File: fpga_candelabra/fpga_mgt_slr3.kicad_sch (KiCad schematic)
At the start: 1 part, among them U1 XCVU13P-B2104

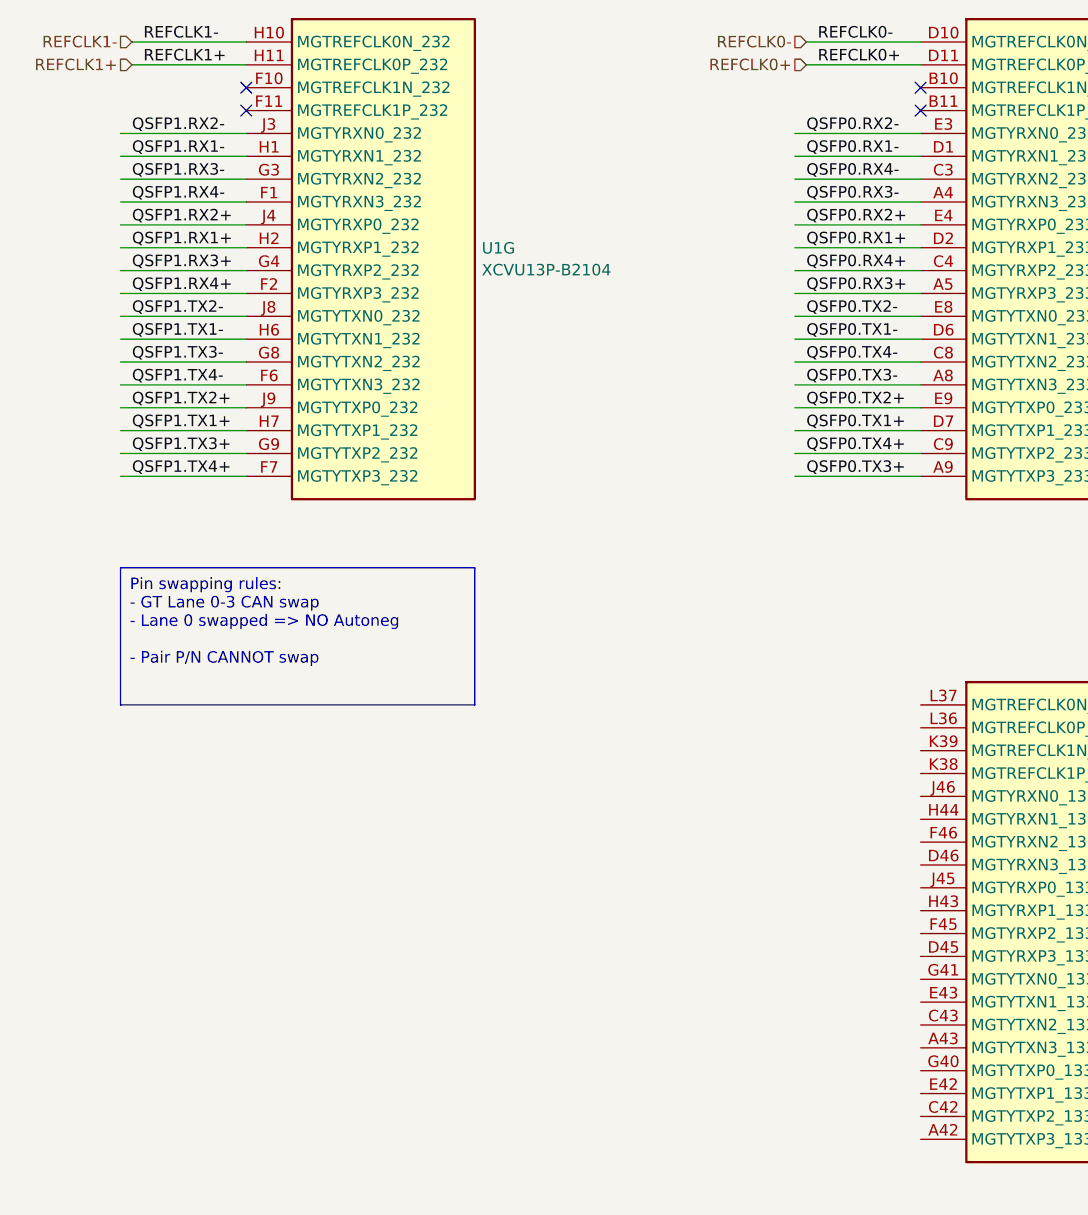
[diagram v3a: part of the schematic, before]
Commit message: fpga_candelabra: sch & layout v0.5, pass basic ERC & DRC
Signed-off-by: Yichuan Gao <gaoyichuan000@gmail.com>
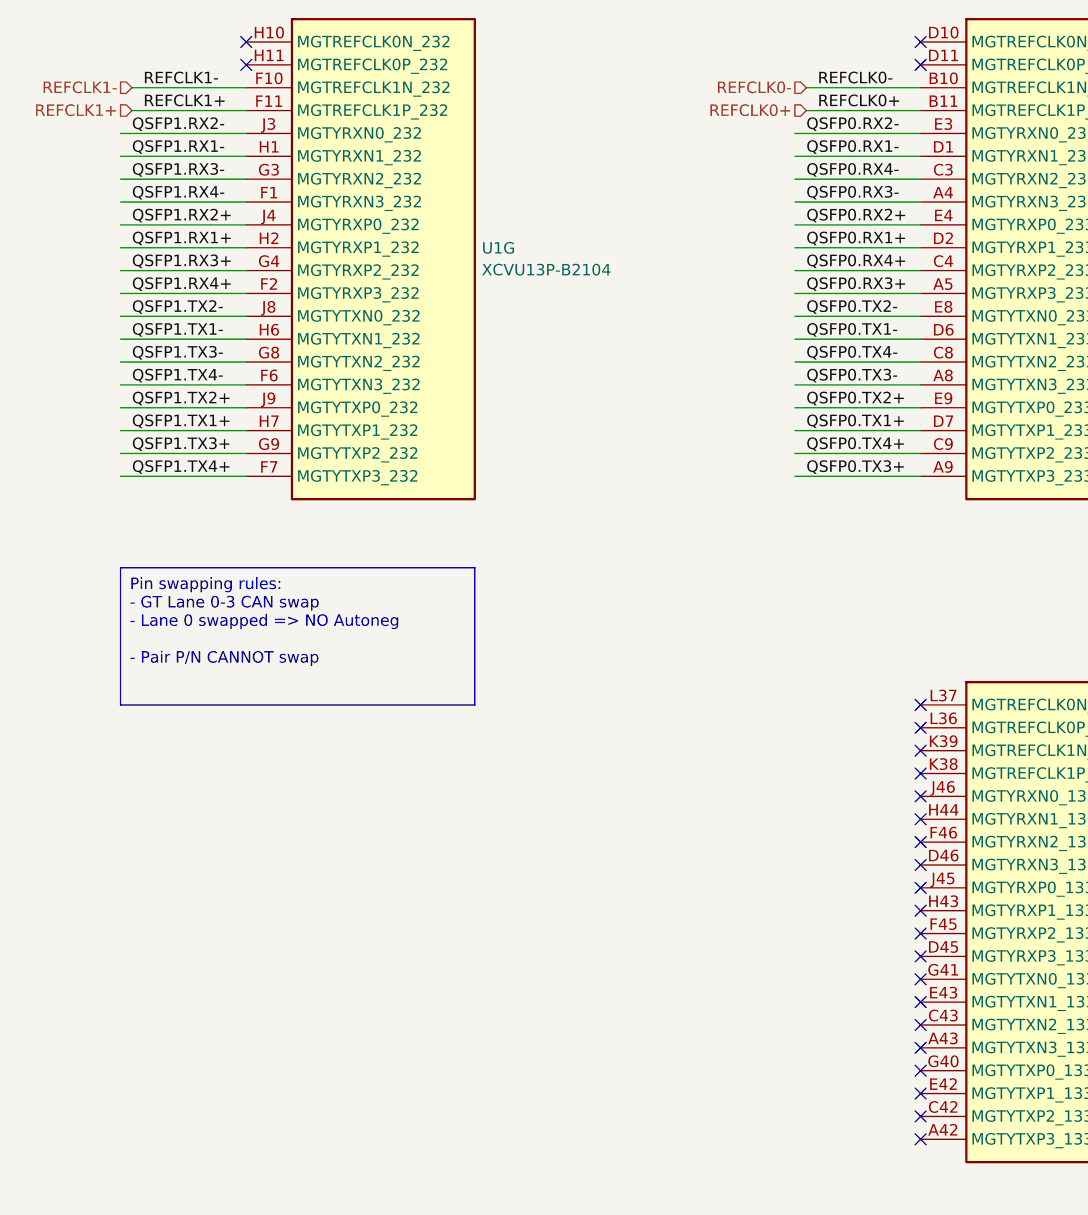
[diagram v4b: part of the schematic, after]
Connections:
- net REFCLK0+: now also U1.B11 (MGTREFCLK1P_233); no longer U1.D11 (MGTREFCLK0P_233)
- net REFCLK0-: now also U1.B10 (MGTREFCLK1N_233); no longer U1.D10 (MGTREFCLK0N_233)
- net REFCLK1+: now also U1.F11 (MGTREFCLK1P_232); no longer U1.H11 (MGTREFCLK0P_232)
- net REFCLK1-: now also U1.F10 (MGTREFCLK1N_232); no longer U1.H10 (MGTREFCLK0N_232)
- no-connect marks 4 -> 24
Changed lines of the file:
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@@
 	(paper "A4")
 	(no_connect
-		(at 45.72 41.91)
-	)
-	(no_connect
-		(at 120.65 39.37)
-	)
-	(no_connect
-		(at 45.72 39.37)
-	)
-	(no_connect
-		(at 120.65 41.91)
+		(at 120.65 115.57)
+	)
+	(no_connect
+		(at 120.65 125.73)
+	)
+	(no_connect
+		(at 120.65 118.11)
+	)
+	(no_connect
+		(at 45.72 36.83)
+	)
+	(no_connect
+		(at 120.65 140.97)
+	)
+	(no_connect
+		(at 120.65 107.95)
+	)
+	(no_connect
+		(at 120.65 146.05)
+	)
+	(no_connect
+		(at 120.65 148.59)
+	)
+	(no_connect
+		(at 120.65 128.27)
+	)
+	(no_connect
+		(at 120.65 110.49)
+	)
+	(no_connect
+		(at 120.65 156.21)
+	)
+	(no_connect
+		(at 120.65 138.43)
+	)
+	(no_connect
+		(at 120.65 123.19)
+	)
+	(no_connect
+		(at 120.65 143.51)
+	)
+	(no_connect
+		(at 120.65 34.29)
+	)
+	(no_connect
+		(at 120.65 113.03)
+	)
+	(no_connect
+		(at 120.65 120.65)
+	)
+	(no_connect
+		(at 120.65 130.81)
+	)
+	(no_connect
+		(at 45.72 34.29)
+	)
+	(no_connect
+		(at 120.65 151.13)
+	)
+	(no_connect
+		(at 120.65 133.35)
+	)
+	(no_connect
+		(at 120.65 36.83)
+	)
+	(no_connect
+		(at 120.65 153.67)
+	)
+	(no_connect
+		(at 120.65 135.89)
 	)
 	(wire
@@
 	(wire
 		(pts
-			(xy 33.02 36.83) (xy 45.72 36.83)
+			(xy 33.02 41.91) (xy 45.72 41.91)
 		)
 		(stroke
@@
 	(wire
 		(pts
-			(xy 107.95 34.29) (xy 120.65 34.29)
+			(xy 107.95 39.37) (xy 120.65 39.37)
 		)
 		(stroke
@@
 	(wire
 		(pts
-			(xy 33.02 34.29) (xy 45.72 34.29)
+			(xy 33.02 39.37) (xy 45.72 39.37)
 		)
 		(stroke
@@
 	(wire
 		(pts
-			(xy 107.95 36.83) (xy 120.65 36.83)
+			(xy 107.95 41.91) (xy 120.65 41.91)
 		)
 		(stroke
@@
 	)
 	(label "REFCLK0-"
-		(at 109.22 34.29 0)
+		(at 109.22 39.37 0)
 		(fields_autoplaced yes)
 		(effects
@@
 	)
 	(label "REFCLK1+"
-		(at 34.29 36.83 0)
+		(at 34.29 41.91 0)
 		(fields_autoplaced yes)
 		(effects
@@
 	)
 	(label "REFCLK1-"
-		(at 34.29 34.29 0)
+		(at 34.29 39.37 0)
 		(fields_autoplaced yes)
 		(effects
@@
 	)
 	(label "REFCLK0+"
-		(at 109.22 36.83 0)
+		(at 109.22 41.91 0)
 		(fields_autoplaced yes)
 		(effects
@@
 	(hierarchical_label "REFCLK0+"
 		(shape input)
-		(at 107.95 36.83 180)
+		(at 107.95 41.91 180)
 		(fields_autoplaced yes)
 		(effects
@@
 	(hierarchical_label "REFCLK1-"
 		(shape input)
-		(at 33.02 34.29 180)
+		(at 33.02 39.37 180)
 		(fields_autoplaced yes)
 		(effects
@@
 	(hierarchical_label "REFCLK1+"
 		(shape input)
-		(at 33.02 36.83 180)
+		(at 33.02 41.91 180)
 		(fields_autoplaced yes)
 		(effects
@@
 	(hierarchical_label "REFCLK0-"
 		(shape input)
-		(at 107.95 34.29 180)
-		(fields_autoplaced yes)
-		(effects
+		(at 107.95 39.37 180)
+		(fields_autoplaced yes)
+		(effects

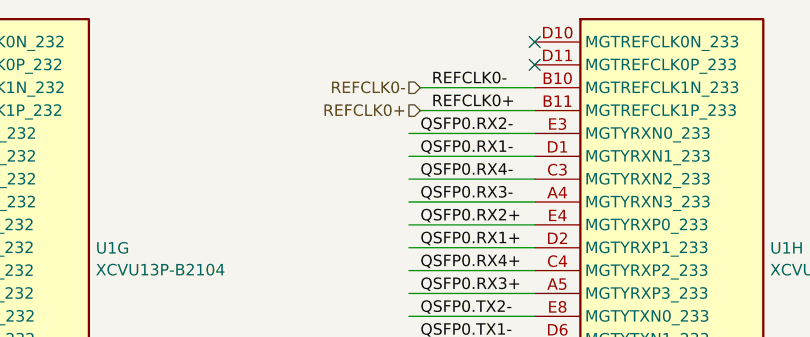
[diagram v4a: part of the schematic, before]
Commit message: fpga_candelabra: more bugfixes & improvements for rev 0.2.0
- Add Digilent JTAG-SMT2-NC onboard
- Add fan controller & 4pin fan header
- Use 9pin header for USB2.0
- Misc fixes for structure

Signed-off-by: Yichuan Gao <gaoyichuan000@gmail.com>
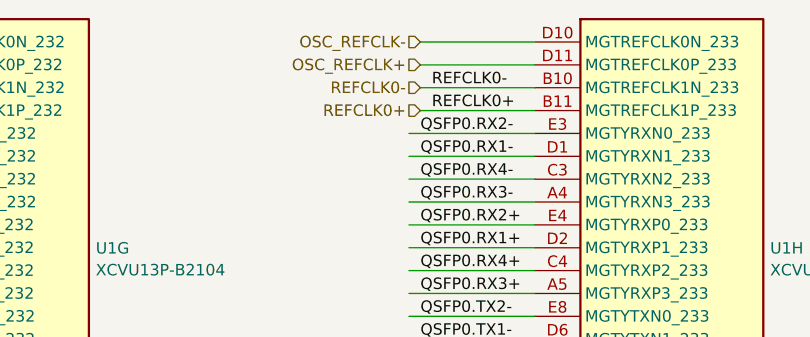
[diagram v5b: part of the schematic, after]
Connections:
- net OSC_REFCLK-: now reaches U1.D10 (MGTREFCLK0N_233)
- net OSC_REFCLK+: now reaches U1.D11 (MGTREFCLK0P_233)
- no-connect marks 24 -> 22
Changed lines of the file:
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@@
-	)
-	(no_connect
-		(at 120.65 34.29)
 	)
 	(no_connect
@@
 	)
 	(no_connect
-		(at 120.65 36.83)
-	)
-	(no_connect
 		(at 120.65 153.67)
 	)
@@
 	(wire
 		(pts
+			(xy 107.95 36.83) (xy 120.65 36.83)
+		)
+		(stroke
+			(width 0)
+			(type default)
+		)
+	)
+	(wire
+		(pts
 			(xy 106.68 82.55) (xy 120.65 82.55)
 		)
@@
 		(pts
 			(xy 31.75 57.15) (xy 45.72 57.15)
+		)
+		(stroke
+			(width 0)
+			(type default)
+		)
+	)
+	(wire
+		(pts
+			(xy 107.95 34.29) (xy 120.65 34.29)
 		)
 		(stroke
@@
 	(label "QSFP1.RX2+"
 		(at 33.02 54.61 0)
-		(fields_autoplaced yes)
 		(effects
 			(font
@@
 	(label "QSFP0.RX2+"
 		(at 107.95 54.61 0)
-		(fields_autoplaced yes)
 		(effects
 			(font
@@
 	(label "QSFP0.TX1-"
 		(at 107.95 67.31 0)
-		(fields_autoplaced yes)
 		(effects
 			(font
@@
 	(label "QSFP0.TX2+"
 		(at 107.95 74.93 0)
-		(fields_autoplaced yes)
 		(effects
 			(font
@@
 	(label "QSFP0.RX4-"
 		(at 107.95 49.53 0)
-		(fields_autoplaced yes)
 		(effects
 			(font
@@
 	(label "QSFP1.RX3+"
 		(at 33.02 59.69 0)
-		(fields_autoplaced yes)
 		(effects
 			(font
@@
 	(label "QSFP0.TX2-"
 		(at 107.95 64.77 0)
-		(fields_autoplaced yes)
 		(effects
 			(font
@@
 	(label "QSFP1.RX1+"
 		(at 33.02 57.15 0)
-		(fields_autoplaced yes)
 		(effects
 			(font
@@
 	(label "QSFP0.TX4+"
 		(at 107.95 80.01 0)
-		(fields_autoplaced yes)
 		(effects
 			(font
@@
 	(label "QSFP1.TX3-"
 		(at 33.02 69.85 0)
-		(fields_autoplaced yes)
 		(effects
 			(font
@@
 	(label "QSFP1.RX2-"
 		(at 33.02 44.45 0)
-		(fields_autoplaced yes)
 		(effects
 			(font
@@
 	(label "QSFP0.RX1+"
 		(at 107.95 57.15 0)
-		(fields_autoplaced yes)
 		(effects
 			(font
@@
 	(label "QSFP0.TX4-"
 		(at 107.95 69.85 0)
-		(fields_autoplaced yes)
 		(effects
 			(font
@@
 	(label "QSFP1.TX1+"
 		(at 33.02 77.47 0)
-		(fields_autoplaced yes)
 		(effects
 			(font
@@
 	(label "QSFP0.TX1+"
 		(at 107.95 77.47 0)
-		(fields_autoplaced yes)
 		(effects
 			(font
@@
 	(label "QSFP0.TX3+"
 		(at 107.95 82.55 0)
-		(fields_autoplaced yes)
 		(effects
 			(font
@@
 	(label "QSFP0.RX3+"
 		(at 107.95 62.23 0)
-		(fields_autoplaced yes)
 		(effects
 			(font
@@
 	(label "REFCLK0-"
 		(at 109.22 39.37 0)
-		(fields_autoplaced yes)
 		(effects
 			(font
@@
 	(label "QSFP1.TX1-"
 		(at 33.02 67.31 0)
-		(fields_autoplaced yes)
 		(effects
 			(font
@@
 	(label "REFCLK1+"
 		(at 34.29 41.91 0)
-		(fields_autoplaced yes)
 		(effects
 			(font
@@
 	(label "QSFP1.RX4+"
 		(at 33.02 62.23 0)
-		(fields_autoplaced yes)
 		(effects
 			(font
@@
 	(label "QSFP1.TX2+"
 		(at 33.02 74.93 0)
-		(fields_autoplaced yes)
 		(effects
 			(font
@@
 	(label "QSFP1.TX4+"
 		(at 33.02 82.55 0)
-		(fields_autoplaced yes)
 		(effects
 			(font
@@
 	(label "QSFP0.TX3-"
 		(at 107.95 72.39 0)
-		(fields_autoplaced yes)
 		(effects
 			(font
@@
 	(label "REFCLK1-"
 		(at 34.29 39.37 0)
-		(fields_autoplaced yes)
 		(effects
 			(font
@@
 	(label "QSFP1.RX1-"
 		(at 33.02 46.99 0)
-		(fields_autoplaced yes)
 		(effects
 			(font
@@
 	(label "QSFP0{QSFP}"
 		(at 265.43 157.48 0)
-		(fields_autoplaced yes)
 		(effects
 			(font
@@
 	(label "QSFP0.RX4+"
 		(at 107.95 59.69 0)
-		(fields_autoplaced yes)
 		(effects
 			(font
@@
 	(label "QSFP1.TX2-"
 		(at 33.02 64.77 0)
-		(fields_autoplaced yes)
 		(effects
 			(font
@@
 	(label "REFCLK0+"
 		(at 109.22 41.91 0)
-		(fields_autoplaced yes)
 		(effects
 			(font
@@
 	(label "QSFP1.TX4-"
 		(at 33.02 72.39 0)
-		(fields_autoplaced yes)
 		(effects
 			(font
@@
 	(label "QSFP0.RX2-"
 		(at 107.95 44.45 0)
-		(fields_autoplaced yes)
 		(effects
 			(font
@@
 	(label "QSFP0.RX3-"
 		(at 107.95 52.07 0)
-		(fields_autoplaced yes)
 		(effects
 			(font
@@
 	(label "QSFP1{QSFP}"
 		(at 265.43 161.29 0)
-		(fields_autoplaced yes)
 		(effects
 			(font
@@
 	(label "QSFP1.RX4-"
 		(at 33.02 52.07 0)
-		(fields_autoplaced yes)
 		(effects
 			(font
@@
 	(label "QSFP1.RX3-"
 		(at 33.02 49.53 0)
-		(fields_autoplaced yes)
 		(effects
 			(font
@@
 	(label "QSFP1.TX3+"
 		(at 33.02 80.01 0)
-		(fields_autoplaced yes)
 		(effects
 			(font
@@
 	(label "QSFP0.RX1-"
 		(at 107.95 46.99 0)
-		(fields_autoplaced yes)
 		(effects
 			(font
@@
 		(shape input)
 		(at 107.95 41.91 180)
-		(fields_autoplaced yes)
 		(effects
 			(font
@@
 		(shape input)
 		(at 33.02 39.37 180)
-		(fields_autoplaced yes)
 		(effects
 			(font
@@
 		(shape input)
 		(at 33.02 41.91 180)
-		(fields_autoplaced yes)
+		(effects
+			(font
+				(size 1.27 1.27)
+			)
+			(justify right)
+		)
+	)
+	(hierarchical_label "OSC_REFCLK+"
+		(shape input)
+		(at 107.95 36.83 180)
 		(effects
 			(font
@@
 		(shape bidirectional)
 		(at 264.16 161.29 180)
-		(fields_autoplaced yes)
 		(effects
 			(font
@@
 		(shape bidirectional)
 		(at 264.16 157.48 180)
-		(fields_autoplaced yes)
+		(effects
+			(font
+				(size 1.27 1.27)
+			)
+			(justify right)
+		)
+	)
+	(hierarchical_label "OSC_REFCLK-"
+		(shape input)
+		(at 107.95 34.29 180)
 		(effects
 			(font
@@
 		(shape input)
 		(at 107.95 39.37 180)
-		(fields_autoplaced yes)
-		(effects
-			(font
+		(effects
+			(font

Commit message: fpga_candelabra: add author & rev to schematics
Signed-off-by: Yichuan Gao <gaoyichuan000@gmail.com>
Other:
- company: (none) -> CHIPS Alliance
- title: (none) -> FPGA SLR3 MGT
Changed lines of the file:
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@@
 	(generator_version "8.0")
 	(paper "A4")
+	(title_block
+		(title "FPGA SLR3 MGT")
+		(date "2025-02-05")
+		(rev "0.2.0")
+		(company "CHIPS Alliance")
+		(comment 1 "Yichuan Gao")
+		(comment 2 "Yichuan Gao")
+	)
 	(no_connect
 		(at 120.65 115.57)

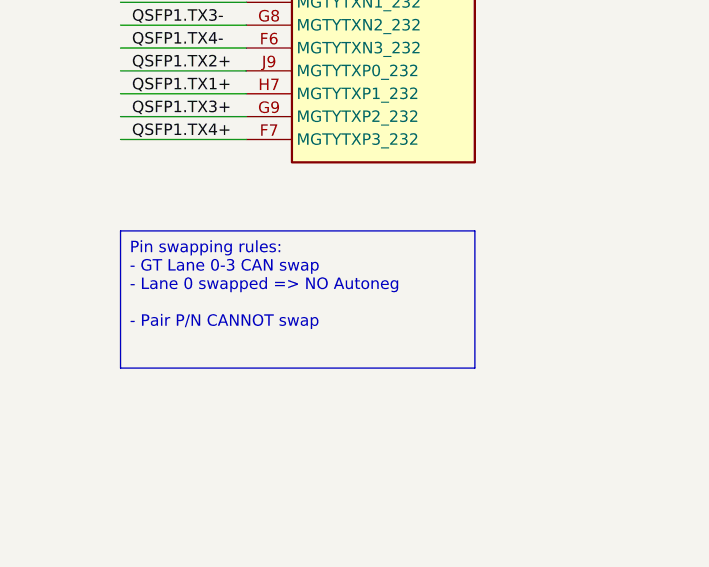
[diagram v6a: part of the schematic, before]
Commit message: fpga_candelabra: update to kicad 9.0
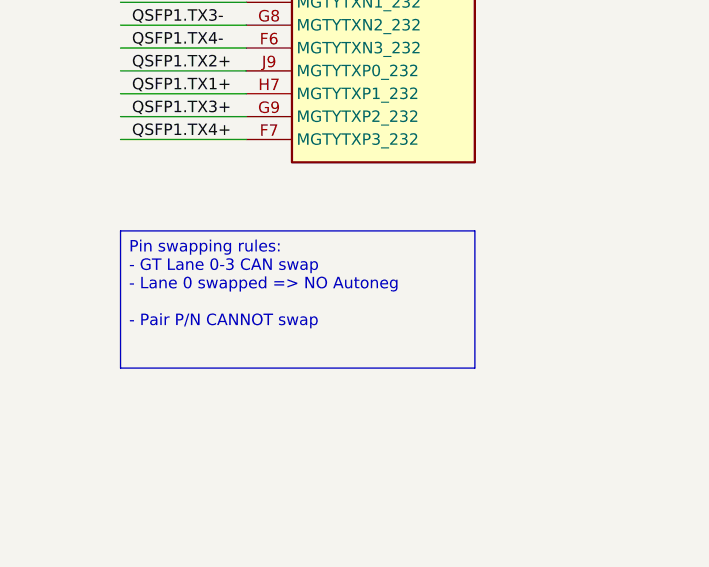
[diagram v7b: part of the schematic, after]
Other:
- company: CHIPS Alliance -> Sipeed
